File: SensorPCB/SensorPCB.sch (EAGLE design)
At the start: 33 parts, among them T1 33u

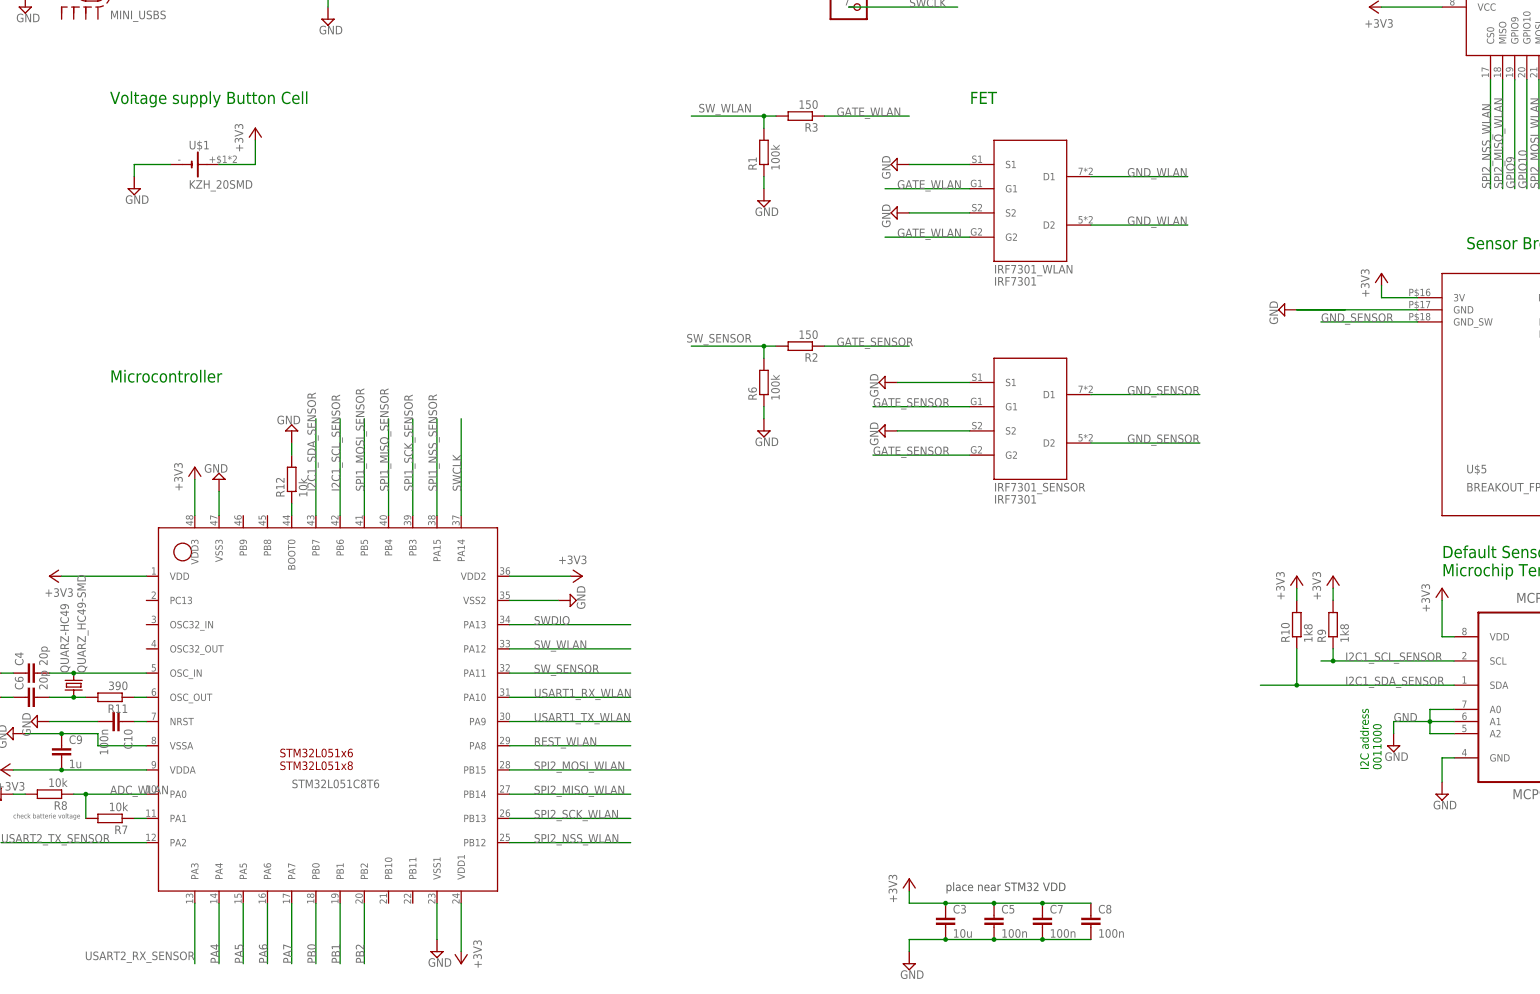
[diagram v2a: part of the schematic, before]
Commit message: i2c pull up
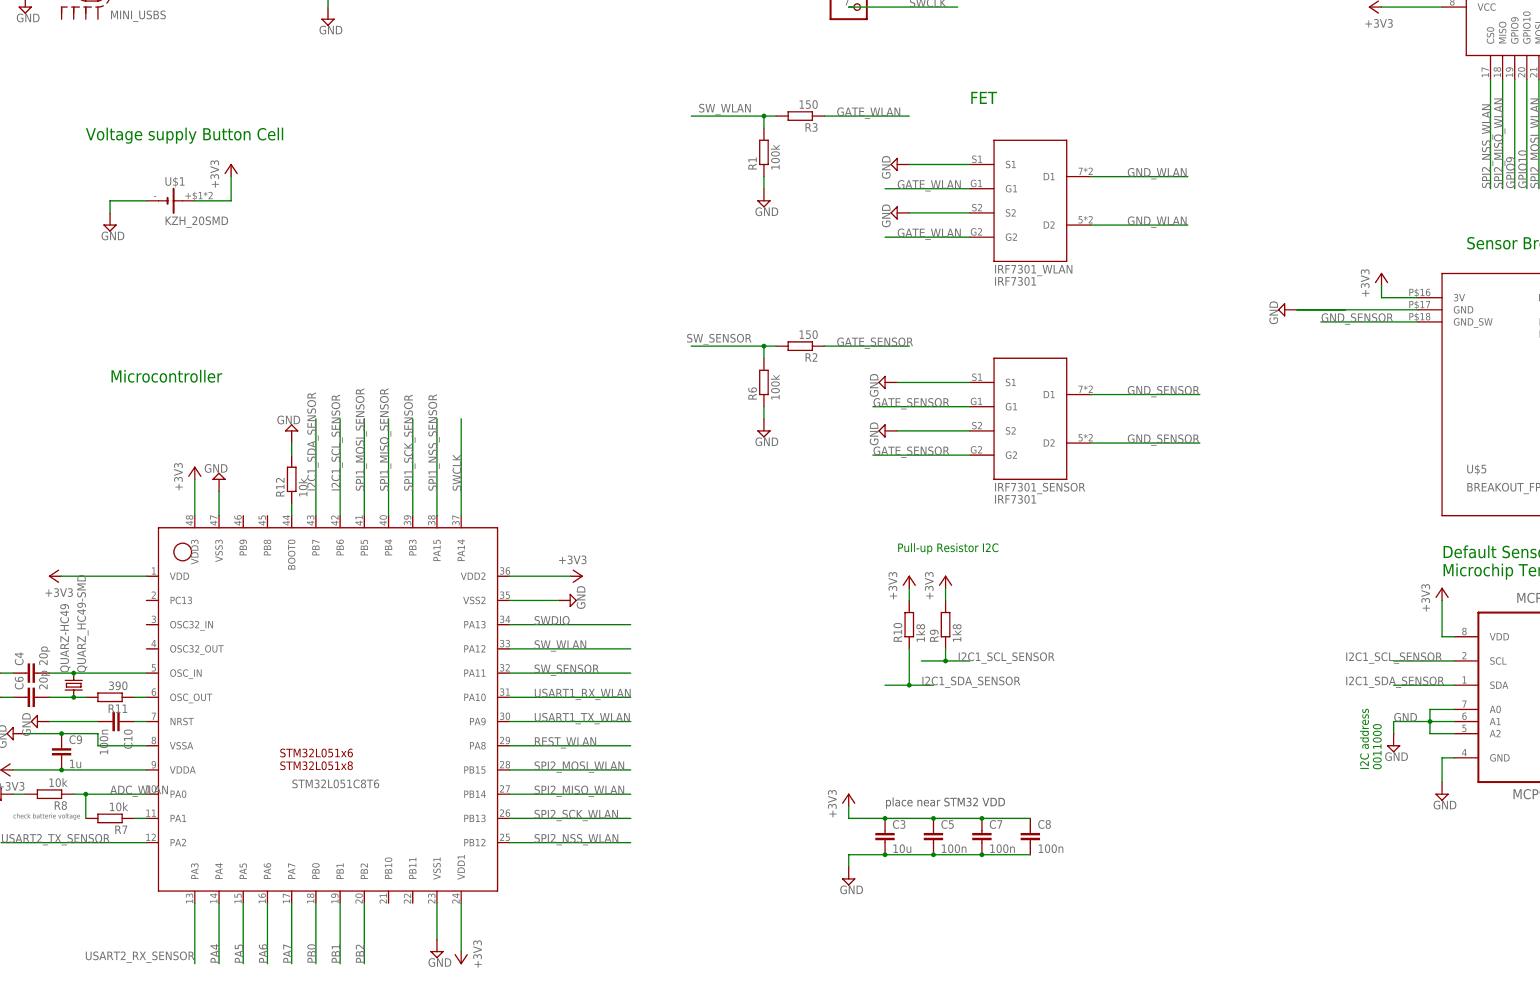
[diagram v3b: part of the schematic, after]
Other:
- note added: "Pull-up Resistor I2C"
- moved on the sheet: C3, C5, C7, C8, R10, R9, U$1
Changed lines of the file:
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@@
 <text x="40.64" y="243.84" size="2.54" layer="91">Voltage supply USB</text>
 <text x="342.9" y="246.38" size="2.54" layer="91" rot="R180">WLAN-module</text>
-<text x="35.56" y="190.5" size="2.54" layer="91">Voltage supply Button Cell</text>
+<text x="30.48" y="182.88" size="2.54" layer="91">Voltage supply Button Cell</text>
 <text x="35.56" y="132.08" size="2.54" layer="91">Microcontroller</text>
 <text x="215.9" y="190.5" size="2.54" layer="91">FET</text>
@@
 <text x="167.64" y="246.38" size="1.778" layer="91">UART Debugging</text>
 <text x="198.12" y="231.14" size="1.778" layer="91">SWD Programming</text>
-<text x="210.82" y="25.4" size="1.778" layer="97">place near STM32 VDD</text>
+<text x="198.12" y="43.18" size="1.778" layer="97">place near STM32 VDD</text>
 <text x="15.24" y="40.64" size="1.016" layer="95">check batterie voltage</text>
 <text x="314.96" y="91.44" size="2.54" layer="91">Default Sensor MCP9808
@@
 <text x="0" y="266.7" size="1.778" layer="94">ADD RESISTORS FOR SPI AND I2C?
 </text>
+<text x="200.66" y="96.52" size="1.778" layer="91">Pull-up Resistor I2C</text>
 </plain>
 <instances>
@@
 <instance part="SUPPLY17" gate="GND" x="73.66" y="121.92" rot="R180"/>
 <instance part="+3V1" gate="G$1" x="299.72" y="210.82" rot="R90"/>
-<instance part="+3V2" gate="G$1" x="203.2" y="27.94"/>
-<instance part="SUPPLY3" gate="GND" x="203.2" y="10.16"/>
+<instance part="+3V2" gate="G$1" x="190.5" y="45.72"/>
+<instance part="SUPPLY3" gate="GND" x="190.5" y="27.94"/>
 <instance part="SUPPLY18" gate="GND" x="172.72" y="170.18"/>
 <instance part="T1" gate="G$1" x="96.52" y="223.52"/>
@@
 <instance part="SUPPLY22" gate="GND" x="314.96" y="45.72"/>
 <instance part="SUPPLY23" gate="GND" x="304.8" y="55.88"/>
-<instance part="+3V10" gate="G$1" x="292.1" y="91.44"/>
-<instance part="+3V11" gate="G$1" x="284.48" y="91.44"/>
+<instance part="+3V10" gate="G$1" x="210.82" y="91.44"/>
+<instance part="+3V11" gate="G$1" x="203.2" y="91.44"/>
 <instance part="C1" gate="G$1" x="66.04" y="223.52"/>
 <instance part="R5" gate="G$1" x="165.1" y="231.14" rot="R90"/>
@@
 <instance part="R2" gate="G$1" x="180.34" y="139.7" rot="R180"/>
 <instance part="R6" gate="G$1" x="172.72" y="132.08" rot="R90"/>
-<instance part="R9" gate="G$1" x="292.1" y="81.28" rot="R90"/>
-<instance part="R10" gate="G$1" x="284.48" y="81.28" rot="R90"/>
-<instance part="C3" gate="G$1" x="210.82" y="20.32"/>
-<instance part="C5" gate="G$1" x="220.98" y="20.32"/>
-<instance part="C7" gate="G$1" x="231.14" y="20.32"/>
-<instance part="C8" gate="G$1" x="241.3" y="20.32"/>
+<instance part="R9" gate="G$1" x="210.82" y="81.28" rot="R90"/>
+<instance part="R10" gate="G$1" x="203.2" y="81.28" rot="R90"/>
+<instance part="C3" gate="G$1" x="198.12" y="38.1"/>
+<instance part="C5" gate="G$1" x="208.28" y="38.1"/>
+<instance part="C7" gate="G$1" x="218.44" y="38.1"/>
+<instance part="C8" gate="G$1" x="228.6" y="38.1"/>
 <instance part="R12" gate="G$1" x="73.66" y="111.76" rot="R90"/>
 <instance part="C4" gate="G$1" x="17.78" y="71.12" rot="R90"/>
@@
 <instance part="R8" gate="G$1" x="22.86" y="45.72" rot="R180"/>
 <instance part="P+1" gate="1" x="17.78" y="231.14"/>
-<instance part="U$1" gate="G$1" x="53.34" y="177.8"/>
-<instance part="+3V15" gate="G$1" x="66.04" y="185.42"/>
-<instance part="SUPPLY24" gate="GND" x="40.64" y="172.72"/>
+<instance part="U$1" gate="G$1" x="48.26" y="170.18"/>
+<instance part="+3V15" gate="G$1" x="60.96" y="177.8"/>
+<instance part="SUPPLY24" gate="GND" x="35.56" y="165.1"/>
 </instances>
 <busses>
@@
 <segment>
 <pinref part="SUPPLY3" gate="GND" pin="GND"/>
-<wire x1="203.2" y1="12.7" x2="203.2" y2="15.24" width="0.1524" layer="91"/>
-<wire x1="203.2" y1="15.24" x2="210.82" y2="15.24" width="0.1524" layer="91"/>
-<wire x1="210.82" y1="15.24" x2="220.98" y2="15.24" width="0.1524" layer="91"/>
+<wire x1="190.5" y1="30.48" x2="190.5" y2="33.02" width="0.1524" layer="91"/>
+<wire x1="190.5" y1="33.02" x2="198.12" y2="33.02" width="0.1524" layer="91"/>
+<wire x1="198.12" y1="33.02" x2="208.28" y2="33.02" width="0.1524" layer="91"/>
 <pinref part="C3" gate="G$1" pin="2"/>
-<junction x="210.82" y="15.24"/>
+<junction x="198.12" y="33.02"/>
 <pinref part="C5" gate="G$1" pin="2"/>
-<wire x1="220.98" y1="15.24" x2="231.14" y2="15.24" width="0.1524" layer="91"/>
-<junction x="220.98" y="15.24"/>
+<wire x1="208.28" y1="33.02" x2="218.44" y2="33.02" width="0.1524" layer="91"/>
+<junction x="208.28" y="33.02"/>
 <pinref part="C7" gate="G$1" pin="2"/>
 <pinref part="C8" gate="G$1" pin="2"/>
-<wire x1="231.14" y1="15.24" x2="241.3" y2="15.24" width="0.1524" layer="91"/>
-<junction x="231.14" y="15.24"/>
+<wire x1="218.44" y1="33.02" x2="228.6" y2="33.02" width="0.1524" layer="91"/>
+<junction x="218.44" y="33.02"/>
 </segment>
 <segment>
@@
 <segment>
 <pinref part="U$1" gate="G$1" pin="-"/>
-<wire x1="48.26" y1="177.8" x2="40.64" y2="177.8" width="0.1524" layer="91"/>
+<wire x1="43.18" y1="170.18" x2="35.56" y2="170.18" width="0.1524" layer="91"/>
 <pinref part="SUPPLY24" gate="GND" pin="GND"/>
-<wire x1="40.64" y1="177.8" x2="40.64" y2="175.26" width="0.1524" layer="91"/>
+<wire x1="35.56" y1="170.18" x2="35.56" y2="167.64" width="0.1524" layer="91"/>
 </segment>
 </net>
@@
 </segment>
 <segment>
-<wire x1="231.14" y1="22.86" x2="220.98" y2="22.86" width="0.1524" layer="91"/>
+<wire x1="218.44" y1="40.64" x2="208.28" y2="40.64" width="0.1524" layer="91"/>
 <pinref part="+3V2" gate="G$1" pin="+3V3"/>
-<wire x1="220.98" y1="22.86" x2="210.82" y2="22.86" width="0.1524" layer="91"/>
-<wire x1="210.82" y1="22.86" x2="203.2" y2="22.86" width="0.1524" layer="91"/>
-<wire x1="203.2" y1="22.86" x2="203.2" y2="25.4" width="0.1524" layer="91"/>
+<wire x1="208.28" y1="40.64" x2="198.12" y2="40.64" width="0.1524" layer="91"/>
+<wire x1="198.12" y1="40.64" x2="190.5" y2="40.64" width="0.1524" layer="91"/>
+<wire x1="190.5" y1="40.64" x2="190.5" y2="43.18" width="0.1524" layer="91"/>
 <pinref part="C3" gate="G$1" pin="1"/>
-<junction x="210.82" y="22.86"/>
+<junction x="198.12" y="40.64"/>
 <pinref part="C5" gate="G$1" pin="1"/>
-<junction x="220.98" y="22.86"/>
+<junction x="208.28" y="40.64"/>
 <pinref part="C7" gate="G$1" pin="1"/>
 <pinref part="C8" gate="G$1" pin="1"/>
-<wire x1="231.14" y1="22.86" x2="241.3" y2="22.86" width="0.1524" layer="91"/>
-<junction x="231.14" y="22.86"/>
+<wire x1="218.44" y1="40.64" x2="228.6" y2="40.64" width="0.1524" layer="91"/>
+<junction x="218.44" y="40.64"/>
 </segment>
 <segment>
@@
 <segment>
 <pinref part="+3V11" gate="G$1" pin="+3V3"/>
-<wire x1="284.48" y1="86.36" x2="284.48" y2="88.9" width="0.1524" layer="91"/>
+<wire x1="203.2" y1="86.36" x2="203.2" y2="88.9" width="0.1524" layer="91"/>
 <pinref part="R10" gate="G$1" pin="2"/>
 </segment>
 <segment>
 <pinref part="+3V10" gate="G$1" pin="+3V3"/>
-<wire x1="292.1" y1="86.36" x2="292.1" y2="88.9" width="0.1524" layer="91"/>
+<wire x1="210.82" y1="86.36" x2="210.82" y2="88.9" width="0.1524" layer="91"/>
 <pinref part="R9" gate="G$1" pin="2"/>
 </segment>
 <segment>
 <pinref part="U$1" gate="G$1" pin="+"/>
-<wire x1="58.42" y1="177.8" x2="66.04" y2="177.8" width="0.1524" layer="91"/>
+<wire x1="53.34" y1="170.18" x2="60.96" y2="170.18" width="0.1524" layer="91"/>
 <pinref part="+3V15" gate="G$1" pin="+3V3"/>
-<wire x1="66.04" y1="182.88" x2="66.04" y2="177.8" width="0.1524" layer="91"/>
+<wire x1="60.96" y1="175.26" x2="60.96" y2="170.18" width="0.1524" layer="91"/>
 </segment>
 </net>
@@
 </segment>
 <segment>
+<wire x1="210.82" y1="76.2" x2="210.82" y2="73.66" width="0.1524" layer="91"/>
+<pinref part="R9" gate="G$1" pin="1"/>
+<wire x1="210.82" y1="73.66" x2="215.9" y2="73.66" width="0.1524" layer="91"/>
+<junction x="210.82" y="73.66"/>
+<label x="213.36" y="73.66" size="1.778" layer="95"/>
+<wire x1="210.82" y1="73.66" x2="205.74" y2="73.66" width="0.1524" layer="91"/>
+</segment>
+<segment>
 <pinref part="MCP9808" gate="A" pin="SCL"/>
-<wire x1="317.5" y1="73.66" x2="292.1" y2="73.66" width="0.1524" layer="91"/>
-<wire x1="292.1" y1="73.66" x2="289.56" y2="73.66" width="0.1524" layer="91"/>
-<wire x1="292.1" y1="76.2" x2="292.1" y2="73.66" width="0.1524" layer="91"/>
-<junction x="292.1" y="73.66"/>
+<wire x1="317.5" y1="73.66" x2="304.8" y2="73.66" width="0.1524" layer="91"/>
 <label x="294.64" y="73.66" size="1.778" layer="95"/>
-<pinref part="R9" gate="G$1" pin="1"/>
 </segment>
 </net>
@@
 </segment>
 <segment>
+<wire x1="203.2" y1="68.58" x2="203.2" y2="76.2" width="0.1524" layer="91"/>
+<pinref part="R10" gate="G$1" pin="1"/>
+<wire x1="203.2" y1="68.58" x2="208.28" y2="68.58" width="0.1524" layer="91"/>
+<junction x="203.2" y="68.58"/>
+<label x="205.74" y="68.58" size="1.778" layer="95"/>
+<wire x1="203.2" y1="68.58" x2="198.12" y2="68.58" width="0.1524" layer="91"/>
+</segment>
+<segment>
 <pinref part="MCP9808" gate="A" pin="SDA"/>
-<wire x1="317.5" y1="68.58" x2="284.48" y2="68.58" width="0.1524" layer="91"/>
-<wire x1="284.48" y1="68.58" x2="284.48" y2="76.2" width="0.1524" layer="91"/>
-<wire x1="284.48" y1="68.58" x2="276.86" y2="68.58" width="0.1524" layer="91"/>
-<junction x="284.48" y="68.58"/>
+<wire x1="317.5" y1="68.58" x2="304.8" y2="68.58" width="0.1524" layer="91"/>
 <label x="294.64" y="68.58" size="1.778" layer="95"/>
-<pinref part="R10" gate="G$1" pin="1"/>
-</segment>
-</net>
+</segment>
+</net>

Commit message: prepare layout
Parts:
- removed R4, R5: 100k, rcl:R-EU_R0805
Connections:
- net N$5 renamed OSC_IN
- net N$6 renamed OSC_OUT
- removed net RX_ICP: PHD.2, R5.1
- removed net TXD_ICP: PHD.1, R4.1
- net +3V3: no longer R4.2, R5.2
- net USART2_RX_SENSOR: now also PHD.2
- net USART2_TX_SENSOR: now also PHD.1
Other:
- note added: "Pull-up I2c"
- note added: "check battery voltage"
- note removed: "ADD RESISTORS FOR SPI AND I2C?"
- note removed: "Pull-up Resistor I2C"
- note removed: "check batterie voltage"
- moved on the sheet: C3, C5, C7, C8, R10, R9, U$1

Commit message: some updates
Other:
- note added: "Pull-up I2C"
- note added: "Second Default Sensor?"
- note added: "dont need the pullup right?"
- note removed: "Pull-up I2c"
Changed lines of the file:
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@@
 <text x="302.26" y="50.8" size="1.778" layer="91" rot="R90">I2C address
 0011000</text>
-<text x="91.44" y="190.5" size="1.778" layer="91">Pull-up I2c</text>
+<text x="91.44" y="190.5" size="1.778" layer="91">Pull-up I2C</text>
+<text x="238.76" y="251.46" size="5.08" layer="94" rot="R180">dont need the pullup right?</text>
+<text x="198.12" y="83.82" size="2.54" layer="91">Second Default Sensor?</text>
 </plain>
 <instances>

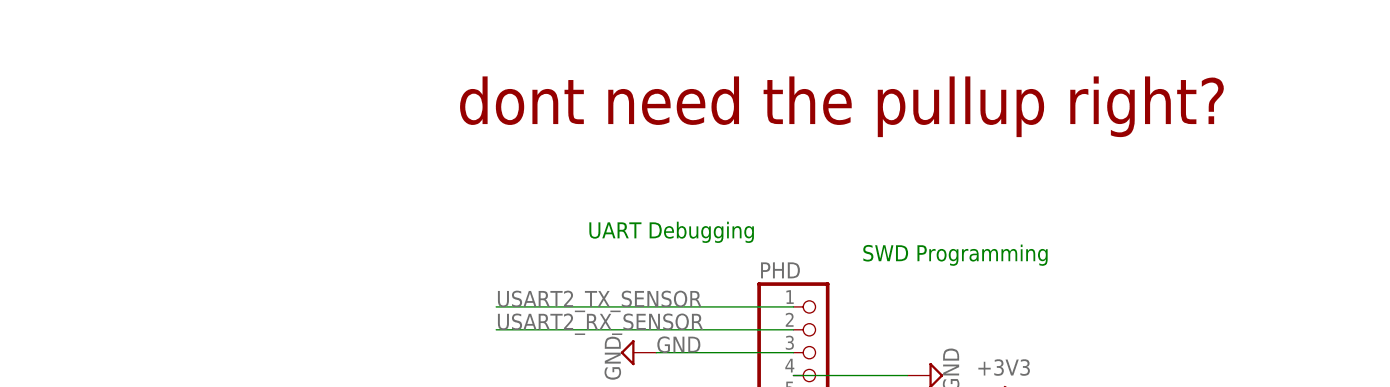
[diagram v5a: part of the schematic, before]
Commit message: routed all signal wires, 3v and GND are absent
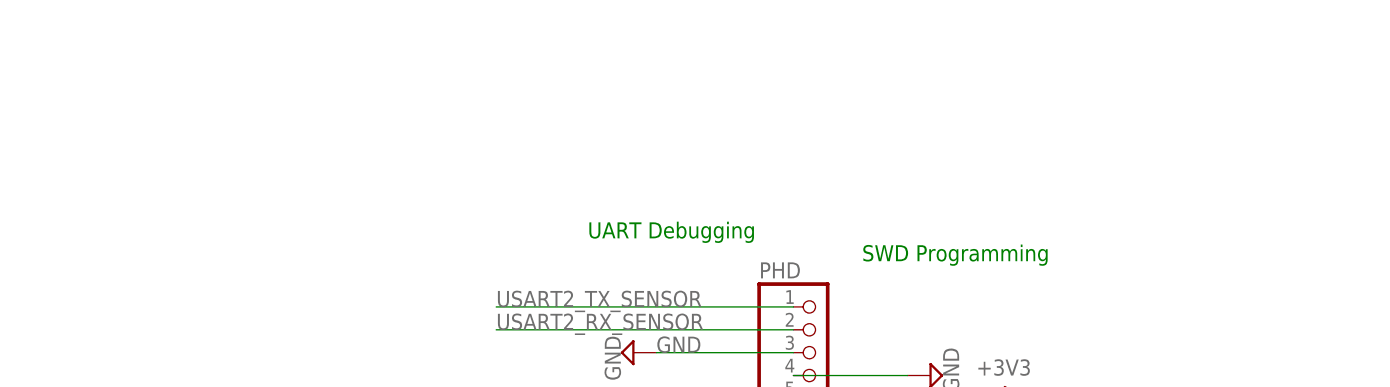
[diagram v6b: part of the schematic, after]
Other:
- note removed: "dont need the pullup right?"
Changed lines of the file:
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@@
 0011000</text>
 <text x="91.44" y="190.5" size="1.778" layer="91">Pull-up I2C</text>
-<text x="238.76" y="251.46" size="5.08" layer="94" rot="R180">dont need the pullup right?</text>
 <text x="198.12" y="83.82" size="2.54" layer="91">Second Default Sensor?</text>
 </plain>

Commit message: start new board version
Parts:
- removed MINI_USB: MINI-USB-SCHIELD-32005-201, con-cypressindustries:MINI-USB-SCHIELD-32005-201
- added R4: 10k, rcl:R-EU_R0805
- added U$2: 5V_POWER_SUPPLY, 5V_POWER_SUPPLY:5V_POWER_SUPPLY
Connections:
- removed net CH_PD_WLAN: ESP8266.CH_PD
- removed net D+: MINI_USBG$1.3
- removed net D-: MINI_USBG$1.2
- removed net ID: MINI_USBG$1.4
- new net ADC: R7.2, R8.1, STM32L051C8T6.PA0
- new net CHPD: ESP8266.CH_PD, R4.1
- net +3V3: now also R4.2
- net +5V: now also U$2.-; no longer MINI_USBG$1.1
- net ADC_WLAN: no longer R7.2, R8.1, STM32L051C8T6.PA0
- net GND: now also U$2.+; no longer MINI_USBG$1.5
- net SPI2_MISO_WLAN: no longer STM32L051C8T6.PB14
- net SPI2_MOSI_WLAN: no longer STM32L051C8T6.PB15
- net SPI2_NSS_WLAN: no longer STM32L051C8T6.PB12
- net SPI2_SCK_WLAN: no longer STM32L051C8T6.PB13
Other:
- note added: "Voltage supply 5V"
- note removed: "Voltage supply USB"
